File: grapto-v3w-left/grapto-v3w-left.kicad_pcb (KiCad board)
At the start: 2 copper layers, 154.6 x 129.3 mm, 136 parts, among them J1 Conn_01x02_Female, J6 USB_C_Receptacle_USB2.0, J8 Conn_01x06_Male, SW31 SW_SPDT, U1 ACN52840, U2 TPS62822DLC, U3 USBLC6-2SC6, U4 BQ24075RGT

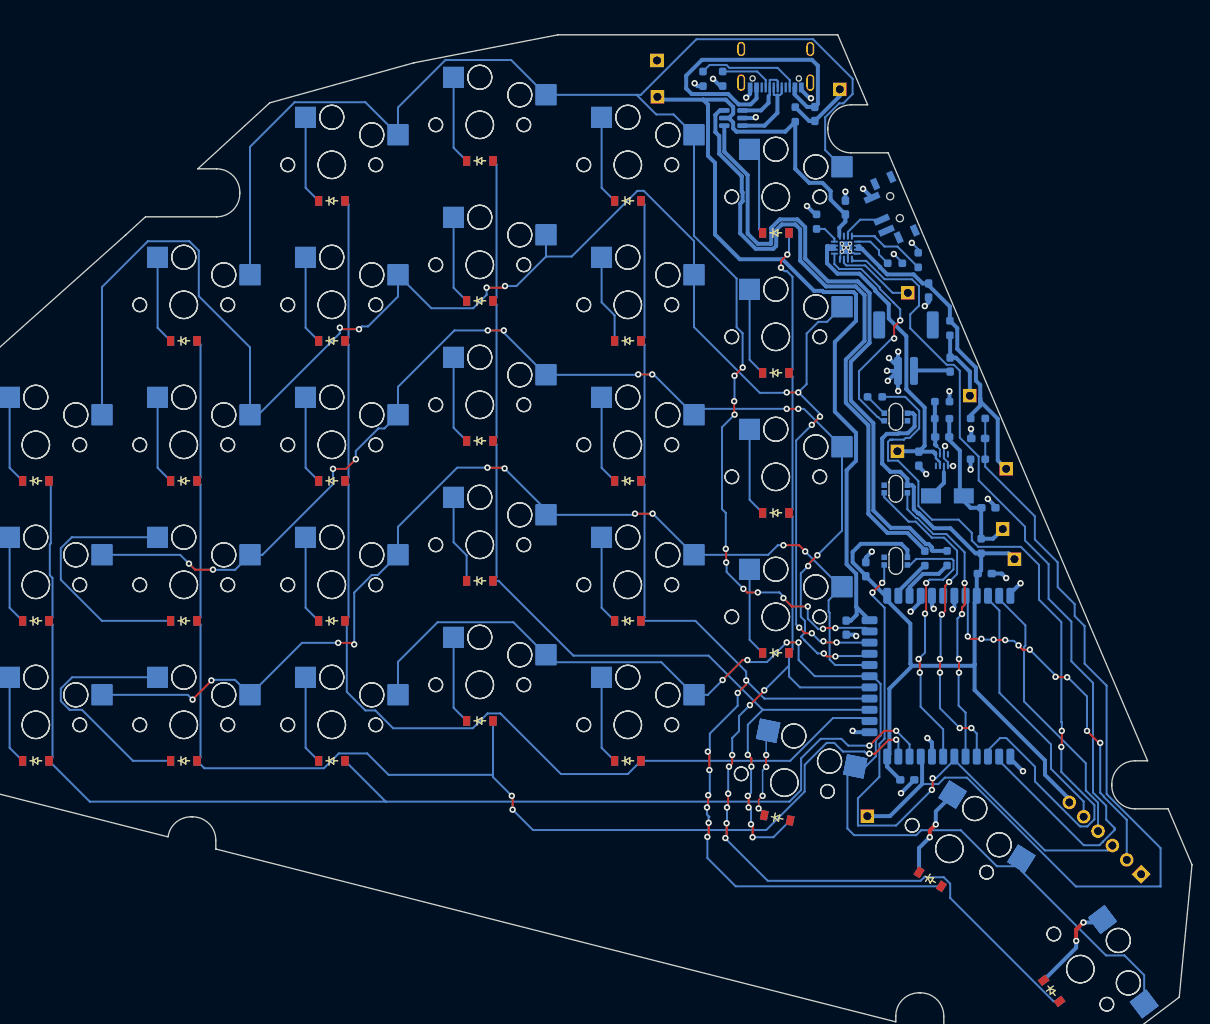
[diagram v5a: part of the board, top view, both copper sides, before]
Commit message: left pcb fix drc.
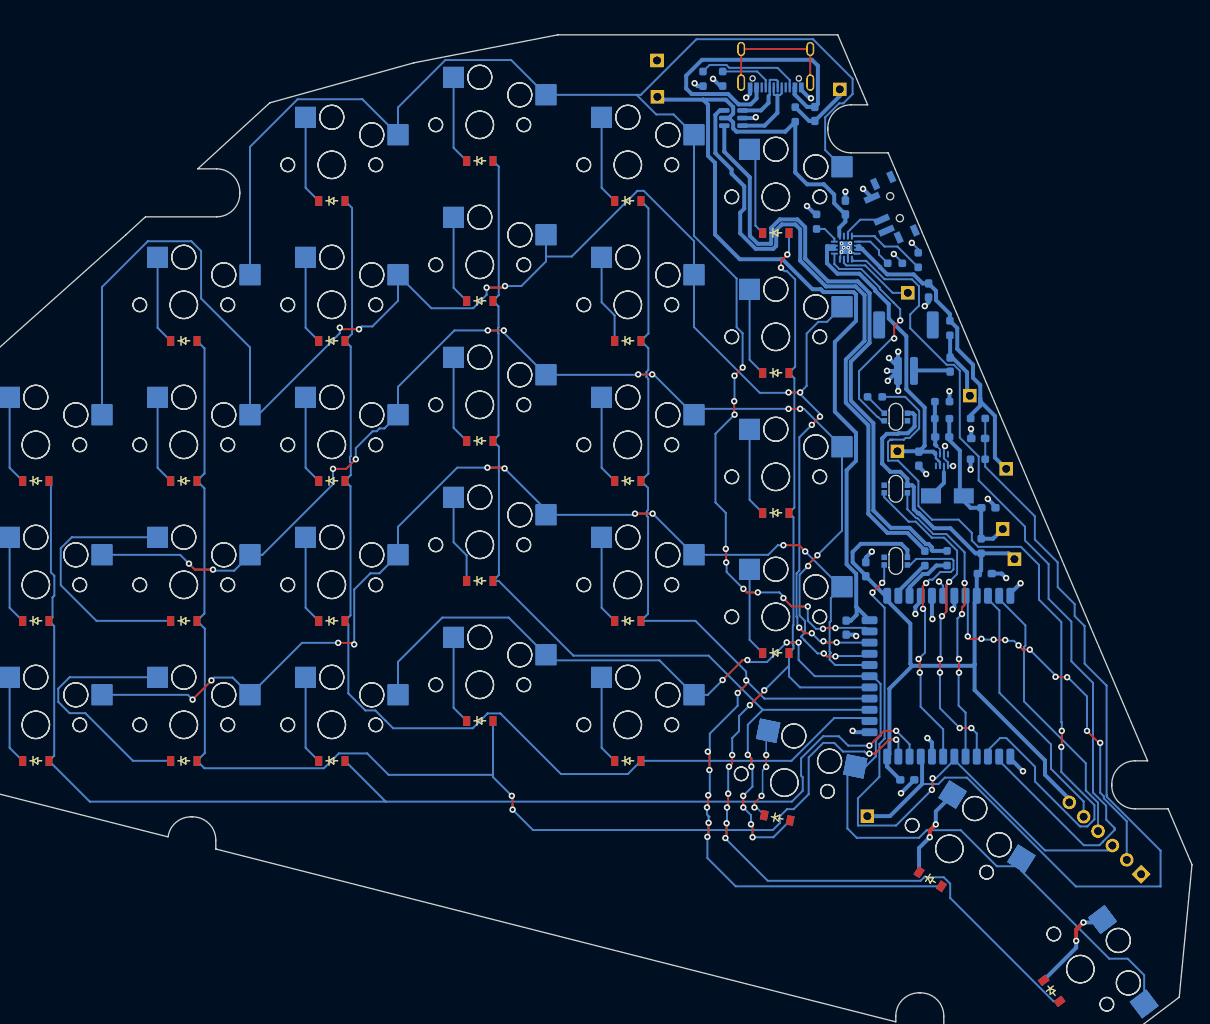
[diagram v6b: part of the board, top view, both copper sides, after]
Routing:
- net /controller/chassi: track 0.00 -> 17.0 mm
- net sysgnd: track 63.4 -> 66.6 mm, vias 40 -> 41
- net col4: track 164.0 -> 166.4 mm
- net col1: track 142.3 -> 143.8 mm
- net col2: track 130.2 -> 131.6 mm
- net row0: track 211.4 -> 212.5 mm
- net col3: track 136.7 -> 137.6 mm
- net col5: track 161.7 -> 162.5 mm
- net row1: track 215.0 -> 215.8 mm
- net row4: track 147.6 -> 148.4 mm
- net col4row3: track 31.1 -> 31.8 mm
- net col0: track 146.3 -> 146.9 mm
- net col2row4: track 11.4 -> 11.9 mm
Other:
- outline, holes or cut-outs redrawn

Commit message: Production files sent to jlcpcb.
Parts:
- added J2: Conn_01x01_Female, TestPoint:TestPoint_THTPad_D2.0mm_Drill1.0mm, B.Cu at (314.0, 98.6)
- C10, C16, C17, C2, C3, C4, C6, C7: footprint Fuse:Fuse_0603_1608Metric_Pad1.05x0.95mm_HandSolder -> Capacitor_SMD:C_0603_1608Metric_Pad1.08x0.95mm_HandSolder
- J6: footprint Connector_USB:USB_C_Receptacle_G-Switch_GT-USB-7010ASV -> grapto-v3w:USB_C_Receptacle_G-Switch_GT-USB-7004
- R1: value 62 -> 68
- TP1, TP10, TP11, TP13, TP14, TP15, TP16, TP17, TP18, TP22: footprint Connector_PinHeader_2.54mm:PinHeader_1x01_P2.54mm_Vertical -> TestPoint:TestPoint_THTPad_D2.0mm_Drill1.0mm
- moved TP14 56.9 mm to (341.4, 153.2)
- moved TP1 11.7 mm to (342.1, 135.4)
- moved R8 10.6 mm to (341.5, 116.0)
- moved TP15 10.6 mm to (307.1, 97.1)
- moved U3 8.98 mm to (318.8, 100.9)
- moved R14 5.63 mm to (350.0, 126.7), turned to 180 degrees
- moved C1 3.43 mm to (337.9, 116.1), turned to 180 degrees
- moved C10 2.93 mm to (349.3, 123.9)
- moved F4 2.22 mm to (336.2, 105.5)
- moved R7 2.02 mm to (337.1, 119.1)
- moved R13 1.81 mm to (333.3, 104.4), turned to 0 degrees
- moved R4 1.47 mm to (346.0, 121.8)
- moved J6 1.15 mm to (332.5, 97.7)
- moved F3 1.07 mm to (354.2, 136.0)
- moved R19 0.94 mm to (356.9, 142.1), turned to -90 degrees
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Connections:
- F4 pad 2: Net-(F4-Pad2) -> vbus_fused
- R13 pad 1: Net-(F4-Pad2) -> vbus_fused
- TP13 pad 1: Net-(F4-Pad2) -> vbus_fused
- U3 pad 5: /controller/vusb -> vbus_fused
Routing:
- net vbus_fused: track 0.00 -> 52.4 mm
- net vbus_no_fuse: track 39.9 -> 10.6 mm
- net cc2: track 12.9 -> 27.8 mm
- net /controller/vusb: track 125.9 -> 112.6 mm, vias 0 -> 2
- net Net-(U4-~{PGOOD}): track 10.0 -> 23.3 mm
- net vsys: track 41.3 -> 54.2 mm
- net USB0_P: track 79.8 -> 92.7 mm
- net USB0_N: track 81.1 -> 93.7 mm
- net row0: track 212.5 -> 224.6 mm
- net usb1_p: track 9.97 -> 19.0 mm
- net usb1_n: track 8.42 -> 17.1 mm
- net Net-(F4-Pad2): track 8.41 -> 0.00 mm
- net /controller/chassi: track 17.0 -> 24.9 mm
- net Net-(U4-ISET): track 10.0 -> 2.36 mm
- net Net-(F3-Pad2): track 8.75 -> 15.2 mm
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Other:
- board text added: "3v3"
- board text added: "Grapto-v3w"
- board text added: "Herman Lundkvist 2023"
- board text added: "gnd"
- board text added: "left"
- board text added: "reset"
- board text added: "stat1"
- board text added: "swclk"
- board text added: "swdio"
